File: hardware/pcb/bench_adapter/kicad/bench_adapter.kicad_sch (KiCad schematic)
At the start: 27 parts, among them J2 J2, J3 J3, J4 J4, J5 J5, J6 J6, J6B J6B, J7 J7, J8 J8, T1 T1, T2 T2

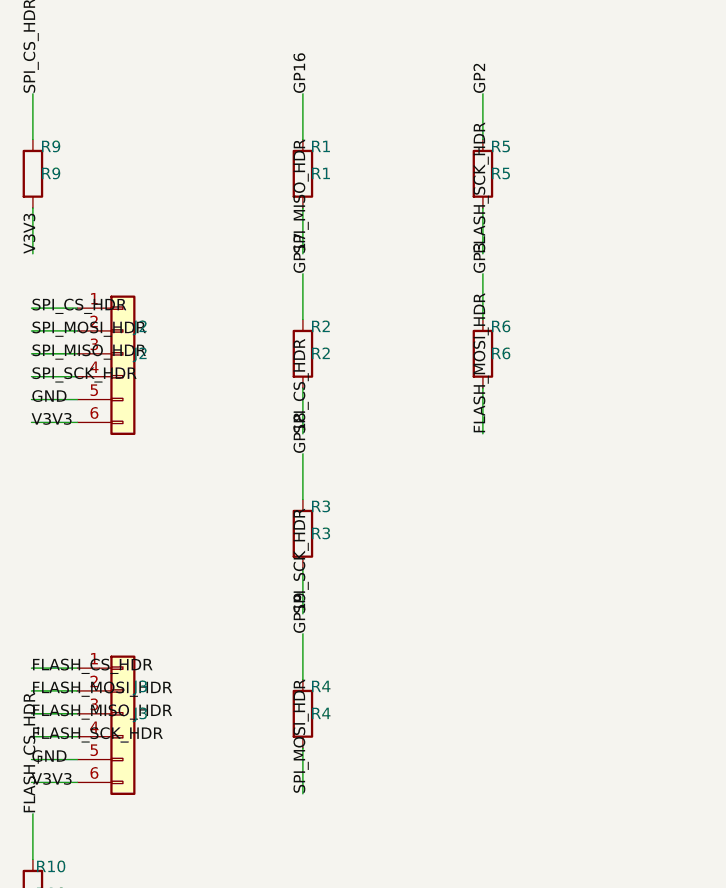
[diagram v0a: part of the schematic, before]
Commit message: bench_adapter: raise J2 SPI series resistors 33R -> 100R for fault-current limiting
RP2350->FPGA SPI backfeed damaged J11 CS/SCK/MOSI on the Wukong A7 (confirmed
via multimeter: 1.0V instead of clean logic levels). 33R was sized for signal
termination (~100mA fault current); 100R caps it at ~33mA. Applied to all four
J2 lines (MISO/CS/SCK/MOSI) for symmetric protection. Flash-PMOD resistors
(R5-R8) stay at 33R since that link never crosses an independent power domain.

Also documents the J11 damage finding and the bench-safety rule (never power
an RP2350 into an unpowered FPGA; 100R inline on jumper-wire SPI hookups
until bench_adapter is fabbed) in AGENTS.md.

Co-Authored-By: Claude Sonnet 5 <noreply@anthropic.com>
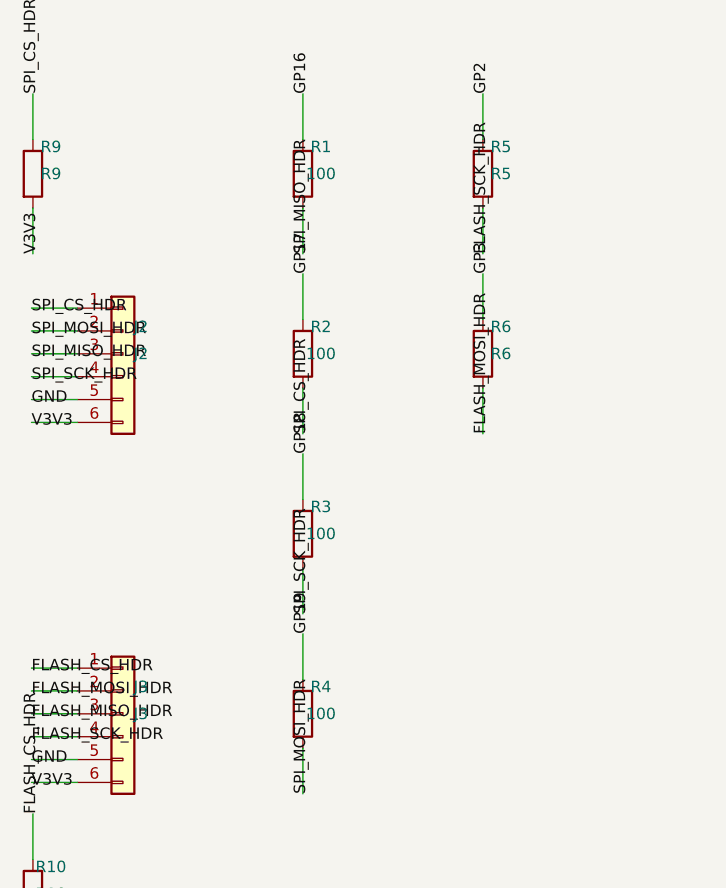
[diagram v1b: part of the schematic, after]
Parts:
- R1: value R1 -> 100
- R2: value R2 -> 100
- R3: value R3 -> 100
- R4: value R4 -> 100
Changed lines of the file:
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@@
     (exclude_from_sim no)(in_bom yes)(on_board yes)(dnp no)
     (property "Reference" "R1" (at 62 17 0) (effects (font (size 1.27 1.27))))
-    (property "Value" "R1" (at 62 20 0) (effects (font (size 1.27 1.27))))
+    (property "Value" "100" (at 62 20 0) (effects (font (size 1.27 1.27))))
     (property "Footprint" "Resistor_THT:R_Axial_DIN0207_L6.3mm_D2.5mm_P10.16mm_Horizontal" (at 60 20 0) (effects (font (size 1.27 1.27)) (hide yes)))
     (property "Datasheet" "" (at 60 20 0) (effects (font (size 1.27 1.27)) (hide yes)))
@@
     (exclude_from_sim no)(in_bom yes)(on_board yes)(dnp no)
     (property "Reference" "R2" (at 62 37 0) (effects (font (size 1.27 1.27))))
-    (property "Value" "R2" (at 62 40 0) (effects (font (size 1.27 1.27))))
+    (property "Value" "100" (at 62 40 0) (effects (font (size 1.27 1.27))))
     (property "Footprint" "Resistor_THT:R_Axial_DIN0207_L6.3mm_D2.5mm_P10.16mm_Horizontal" (at 60 40 0) (effects (font (size 1.27 1.27)) (hide yes)))
     (property "Datasheet" "" (at 60 40 0) (effects (font (size 1.27 1.27)) (hide yes)))
@@
     (exclude_from_sim no)(in_bom yes)(on_board yes)(dnp no)
     (property "Reference" "R3" (at 62 57 0) (effects (font (size 1.27 1.27))))
-    (property "Value" "R3" (at 62 60 0) (effects (font (size 1.27 1.27))))
+    (property "Value" "100" (at 62 60 0) (effects (font (size 1.27 1.27))))
     (property "Footprint" "Resistor_THT:R_Axial_DIN0207_L6.3mm_D2.5mm_P10.16mm_Horizontal" (at 60 60 0) (effects (font (size 1.27 1.27)) (hide yes)))
     (property "Datasheet" "" (at 60 60 0) (effects (font (size 1.27 1.27)) (hide yes)))
@@
     (exclude_from_sim no)(in_bom yes)(on_board yes)(dnp no)
     (property "Reference" "R4" (at 62 77 0) (effects (font (size 1.27 1.27))))
-    (property "Value" "R4" (at 62 80 0) (effects (font (size 1.27 1.27))))
+    (property "Value" "100" (at 62 80 0) (effects (font (size 1.27 1.27))))
     (property "Footprint" "Resistor_THT:R_Axial_DIN0207_L6.3mm_D2.5mm_P10.16mm_Horizontal" (at 60 80 0) (effects (font (size 1.27 1.27)) (hide yes)))
     (property "Datasheet" "" (at 60 80 0) (effects (font (size 1.27 1.27)) (hide yes)))

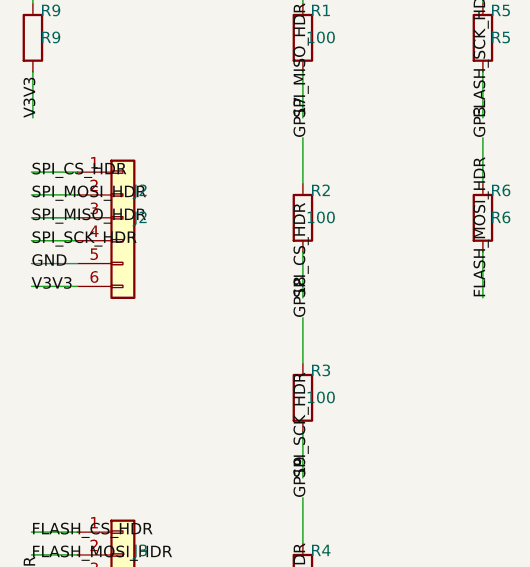
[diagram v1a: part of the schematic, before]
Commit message: pcb: bench_adapter Rev B power-ready interlock design + breadboard proof plan
Direct response to the Wukong J11 backfeed damage confirmed this month:
a powered RP2350 driving CS#/SCK/MOSI into an unpowered FPGA through its
I/O clamp diodes. Rev A relied only on series resistors for fault-current
limiting; Rev B adds a hardware power-ready interlock ahead of them.

J2's four SPI signals now route through U1 (SN74CBTLV3125, Ioff-rated
4-channel bidirectional bus switch), enabled only when U2 (TLV3011B
micropower comparator, fail-safe input) detects the target's 3V3 rail
above a qualified-on threshold. Both are Pico-3V3-powered so the
interlock itself never depends on the target being alive. J2 pin 6 is
renamed TARGET_3V3_SENSE in the schematic and documented as sense-only,
never a rail tie, closing the exact failure mode that damaged the
Wukong's J11 pins.

Adds power_ready_interlock_breadboard.md: the mandatory pre-layout
breadboard bring-up/acceptance sequence for the interlock, and a fresh
bench_adapter.kicad_pcb skeleton. Spec now hands off Rev B tapeout to an
EE reviewer with explicit non-negotiable electrical requirements and
required acceptance evidence, rather than treating this schematic as
final; U1/U2 are documented but not yet captured in the netlist.

Co-Authored-By: Claude Sonnet 5 <noreply@anthropic.com>
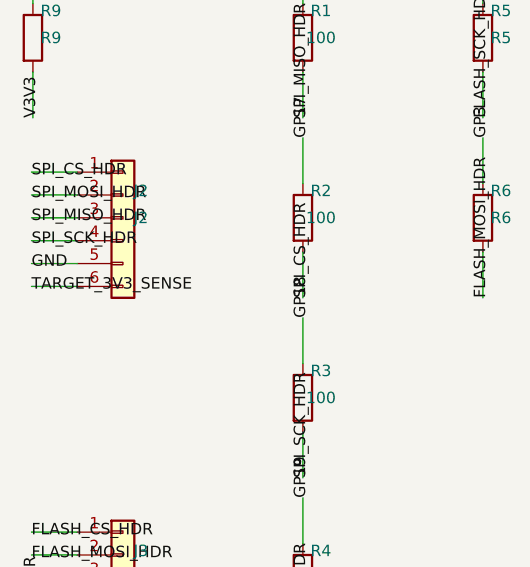
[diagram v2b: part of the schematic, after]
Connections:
- net V3V3: no longer J2.6 (Pin_6)
- new net TARGET_3V3_SENSE: J2.6 (Pin_6)
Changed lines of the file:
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@@
   (label "GND" (at 29.84 45.08 0) (effects (font (size 1.27 1.27))))
   (wire (pts (xy 34.92 47.62) (xy 29.84 47.62)) (stroke (width 0) (type default)))
-  (label "V3V3" (at 29.84 47.62 0) (effects (font (size 1.27 1.27))))
+  (label "TARGET_3V3_SENSE" (at 29.84 47.62 0) (effects (font (size 1.27 1.27))))
   (wire (pts (xy 34.92 74.92) (xy 29.84 74.92)) (stroke (width 0) (type default)))
   (label "FLASH_CS_HDR" (at 29.84 74.92 0) (effects (font (size 1.27 1.27))))

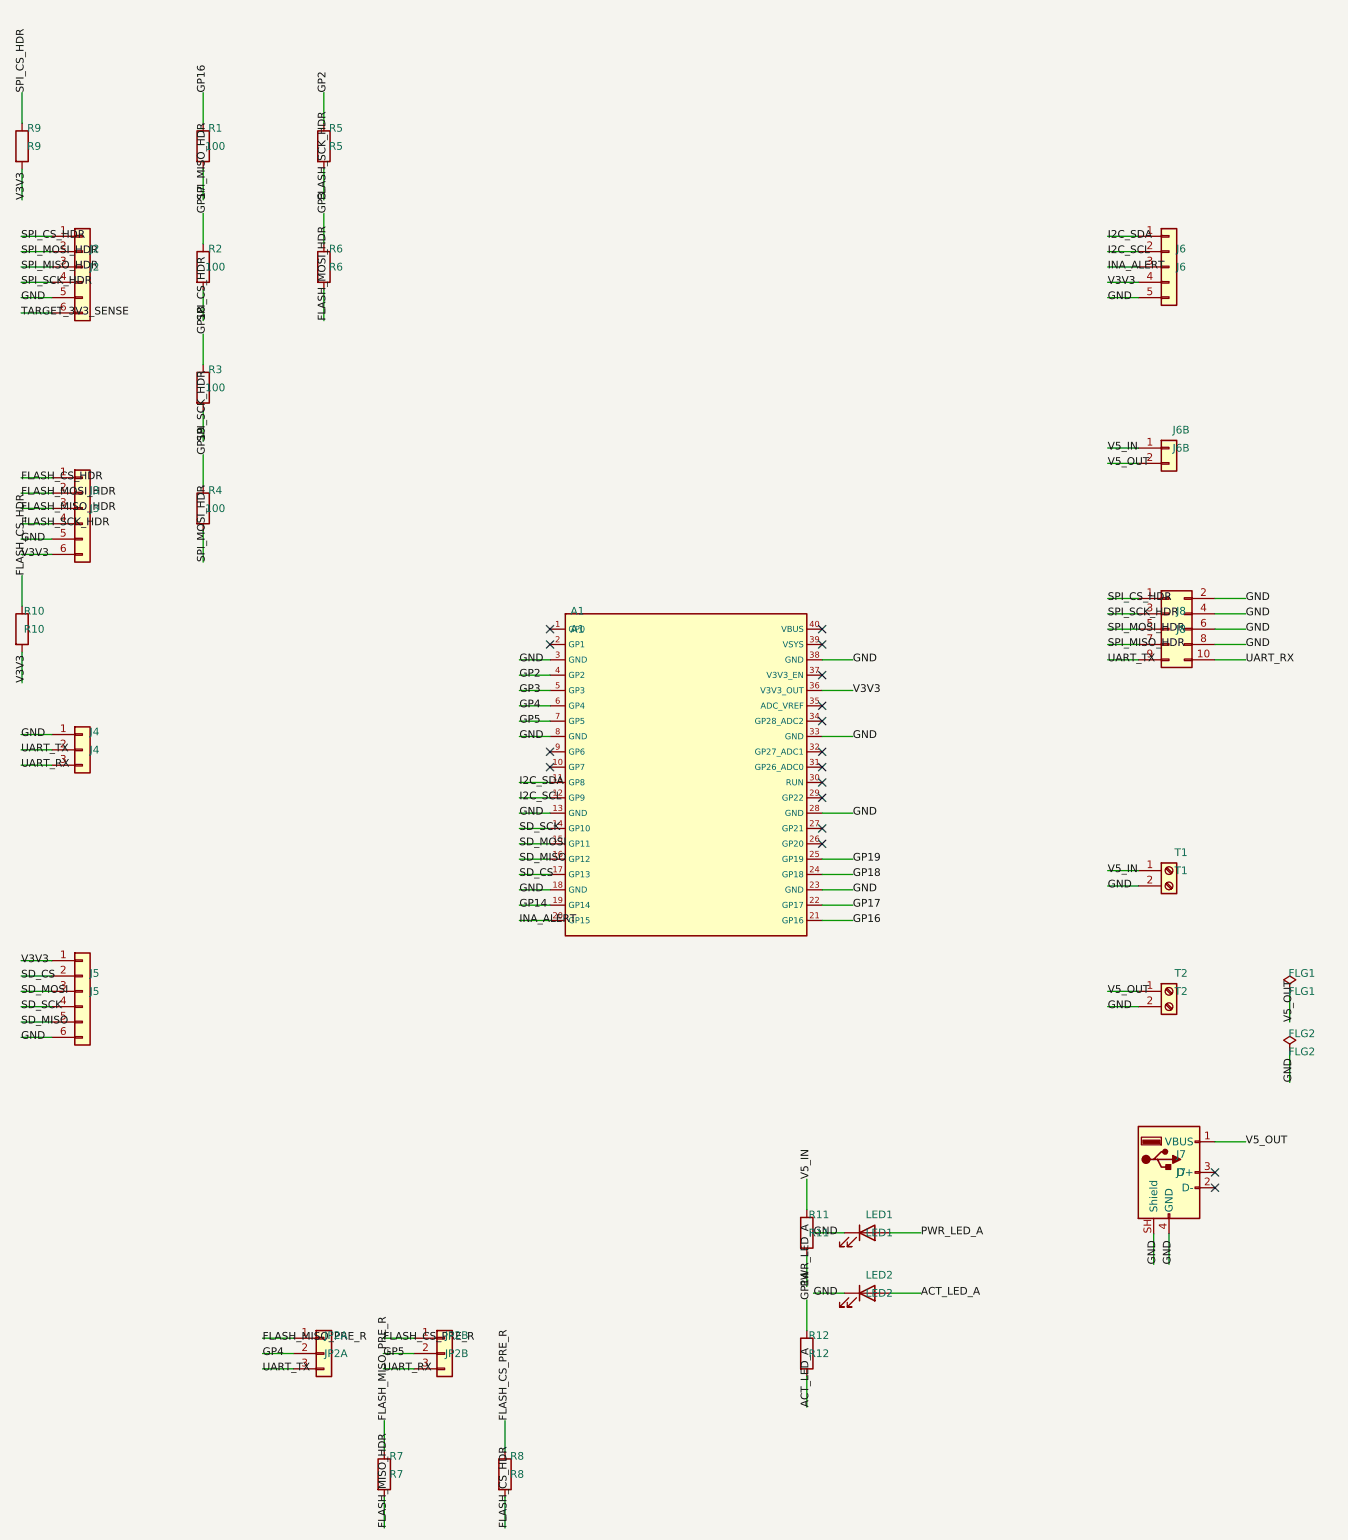
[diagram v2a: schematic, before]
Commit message: pcb: complete bench_adapter schematic -- interlock, Pico 2 footprint, three capture fixes
Schematic goes from Rev A-with-gaps to complete: 37 components, every footprint
assigned, 0 ERC errors. Three captures were wrong against physical parts or
datasheets, and one of them was destructive.

J6 would have destroyed the INA226 module. Three sources disagreed and all
three were wrong: the schematic had a 1x05 (SDA/SCL/ALERT/VCC/GND), the BOM
described a 6-pin header, and the physical part is a single 1x08 reading
IN+ IN- VBS ALE SCL SDA GND VCC. Seating the real module into the captured
socket would have put the 5 V metering rail onto the I2C lines. J9 is deleted,
J6 is one Conn_01x08 in silkscreen order. VBS was absent from the design
entirely -- it is the bus-voltage sense input, on the channel that failed on
08-07 -- and is tied to IN- to match the breadboard rig, so VBUS keeps reading
the same node and existing captures stay comparable with the frozen
ina226_coarse_monitor_v2.json contract. J5 already guarded against this class
by naming its module order inline; 2.5 now does the same for J6.

JP2 contradicted its own spec. The 07-09 correction says a 2x3 block, "still
one reference designator", qty 1; the capture had two Conn_01x03 symbols on two
1x3 footprints. The 08-10 handover's proposed rename to JP2/JP3 would have
frozen that bug rather than fixed it. Now one Conn_02x03_Odd_Even. Shunts must
bridge along the columns, never across the rows -- across-rows is the default
mental model for a 2x3 and shorts FLASH_MISO_PRE_R to FLASH_CS_PRE_R.

The interlock spec was wrong in three places, found by reading TI SCDS037K and
SBOS300C rather than trusting a search summary, which returned an inverted U2
pinout. Polarity resolved: open-drain OUT pulls low when IN- > IN+, so the
divider drives IN- and REF drives IN+. R16 alone would not have worked -- REF
sources 0.5 mA and holds IN+ directly, swamping a 1M feedback -- so R17 (10k)
is added in series from REF; without it t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
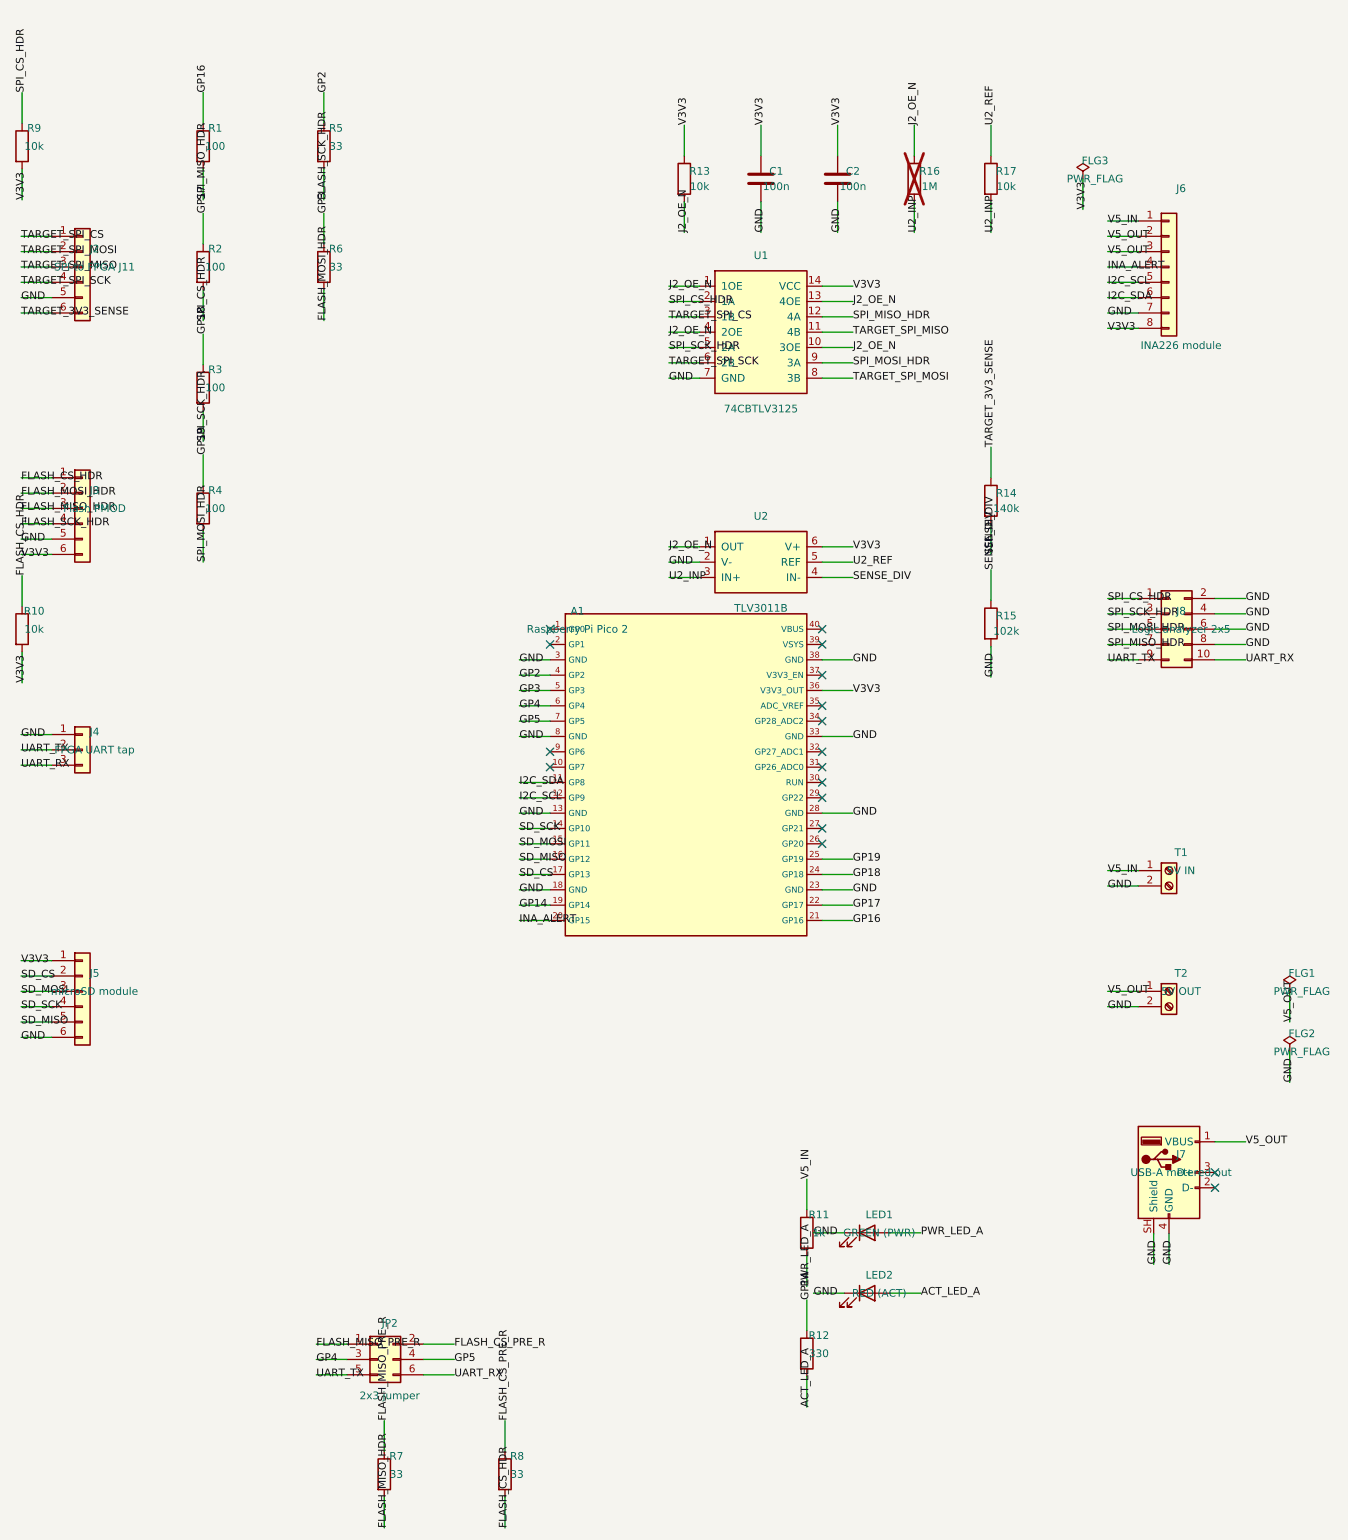
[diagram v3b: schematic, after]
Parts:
- removed J6: J6, Connector_PinSocket_2.54mm:PinSocket_1x05_P2.54mm_Vertical, symbol Connector_Generic:Conn_01x05
- removed J6B: J6B, Connector_PinSocket_2.54mm:PinSocket_1x02_P2.54mm_Vertical, symbol Connector_Generic:Conn_01x02
- removed JP2A: JP2A, Connector_PinHeader_2.54mm:PinHeader_1x03_P2.54mm_Vertical, symbol Connector_Generic:Conn_01x03
- removed JP2B: JP2B, Connector_PinHeader_2.54mm:PinHeader_1x03_P2.54mm_Vertical, symbol Connector_Generic:Conn_01x03
- added C1, C2: 100n, Capacitor_THT:C_Disc_D5.0mm_W2.5mm_P5.00mm, symbol Device:C
- added J6: INA226 module, Connector_PinSocket_2.54mm:PinSocket_1x08_P2.54mm_Vertical, symbol Connector_Generic:Conn_01x08
- added JP2: 2x3 jumper, Connector_PinHeader_2.54mm:PinHeader_2x03_P2.54mm_Vertical, symbol Connector_Generic:Conn_02x03_Odd_Even
- added R13, R17: 10k, Resistor_THT:R_Axial_DIN0207_L6.3mm_D2.5mm_P10.16mm_Horizontal, symbol Device:R
- added R14: 140k, Resistor_THT:R_Axial_DIN0207_L6.3mm_D2.5mm_P10.16mm_Horizontal, symbol Device:R
- added R15: 102k, Resistor_THT:R_Axial_DIN0207_L6.3mm_D2.5mm_P10.16mm_Horizontal, symbol Device:R
- added R16: 1M, Resistor_THT:R_Axial_DIN0207_L6.3mm_D2.5mm_P10.16mm_Horizontal, symbol Device:R
- added U1: 74CBTLV3125, Package_DIP:DIP-14_W7.62mm_Socket, symbol Local:74CBTLV3125
- added U2: TLV3011B, Package_DIP:DIP-6_W7.62mm_Socket, symbol Local:TLV3011B
- A1: value A1 -> Raspberry Pi Pico 2; footprint (none) -> bench_adapter:RPi_Pico2_Module_Socketed
- J2: value J2 -> SPI to FPGA J11
- J3: value J3 -> Flash PMOD
- J4: value J4 -> FPGA UART tap
- J5: value J5 -> microSD module
- J7: value J7 -> USB-A metered out
- J8: value J8 -> Logic analyzer 2x5
- LED1: value LED1 -> GREEN (PWR)
- LED2: value LED2 -> RED (ACT)
- R10: value R10 -> 10k
- R11: value R11 -> 1k
- R12: value R12 -> 330
- R5: value R5 -> 33
- R6: value R6 -> 33
- R7: value R7 -> 33
- R8: value R8 -> 33
- R9: value R9 -> 10k
- T1: value T1 -> 5V IN
- T2: value T2 -> 5V OUT
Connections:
- net FLASH_CS_PRE_R: now also JP2.2 (Pin_2)
- net FLASH_MISO_PRE_R: now also JP2.1 (Pin_1)
- net GND: now also C1.2, C2.2, J6.7 (Pin_7), R15.2, U1.7 (GND), U2.2 (V-)
- net GP4: now also JP2.3 (Pin_3)
- net GP5: now also JP2.4 (Pin_4)
- net I2C_SCL: now also J6.5 (Pin_5)
- net I2C_SDA: now also J6.6 (Pin_6)
- net INA_ALERT: now also J6.4 (Pin_4)
- net SPI_CS_HDR: now also U1.2 (1A); no longer J2.1 (Pin_1)
- net SPI_MISO_HDR: now also U1.12 (4A); no longer J2.3 (Pin_3)
- net SPI_MOSI_HDR: now also U1.9 (3A); no longer J2.2 (Pin_2)
- net SPI_SCK_HDR: now also U1.5 (2A); no longer J2.4 (Pin_4)
- net TARGET_3V3_SENSE: now also R14.1
- net UART_RX: now also JP2.6 (Pin_6)
- net UART_TX: now also JP2.5 (Pin_5)
- net V3V3: now also C1.1, C2.1, J6.8 (Pin_8), R13.1, U1.14 (VCC), U2.6 (V+)
- net V5_IN: now also J6.1 (Pin_1)
- net V5_OUT: now also J6.2 (Pin_2), J6.3 (Pin_3)
- new net J2_OE_N: R13.2, R16.1, U1.1 (1OE), U1.10 (3OE), U1.13 (4OE), U1.4 (2OE), U2.1 (OUT)
- new net SENSE_DIV: R14.2, R15.1, U2.4 (IN-)
- new net TARGET_SPI_CS: J2.1 (Pin_1), U1.3 (1B)
- new net TARGET_SPI_MISO: J2.3 (Pin_3), U1.11 (4B)
- new net TARGET_SPI_MOSI: J2.2 (Pin_2), U1.8 (3B)
- new net TARGET_SPI_SCK: J2.4 (Pin_4), U1.6 (2B)
- new net U2_INP: R16.2, R17.2, U2.3 (IN+)
- new net U2_REF: R17.1, U2.5 (REF)
